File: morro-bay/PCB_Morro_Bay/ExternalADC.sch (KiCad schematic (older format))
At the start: 8 parts

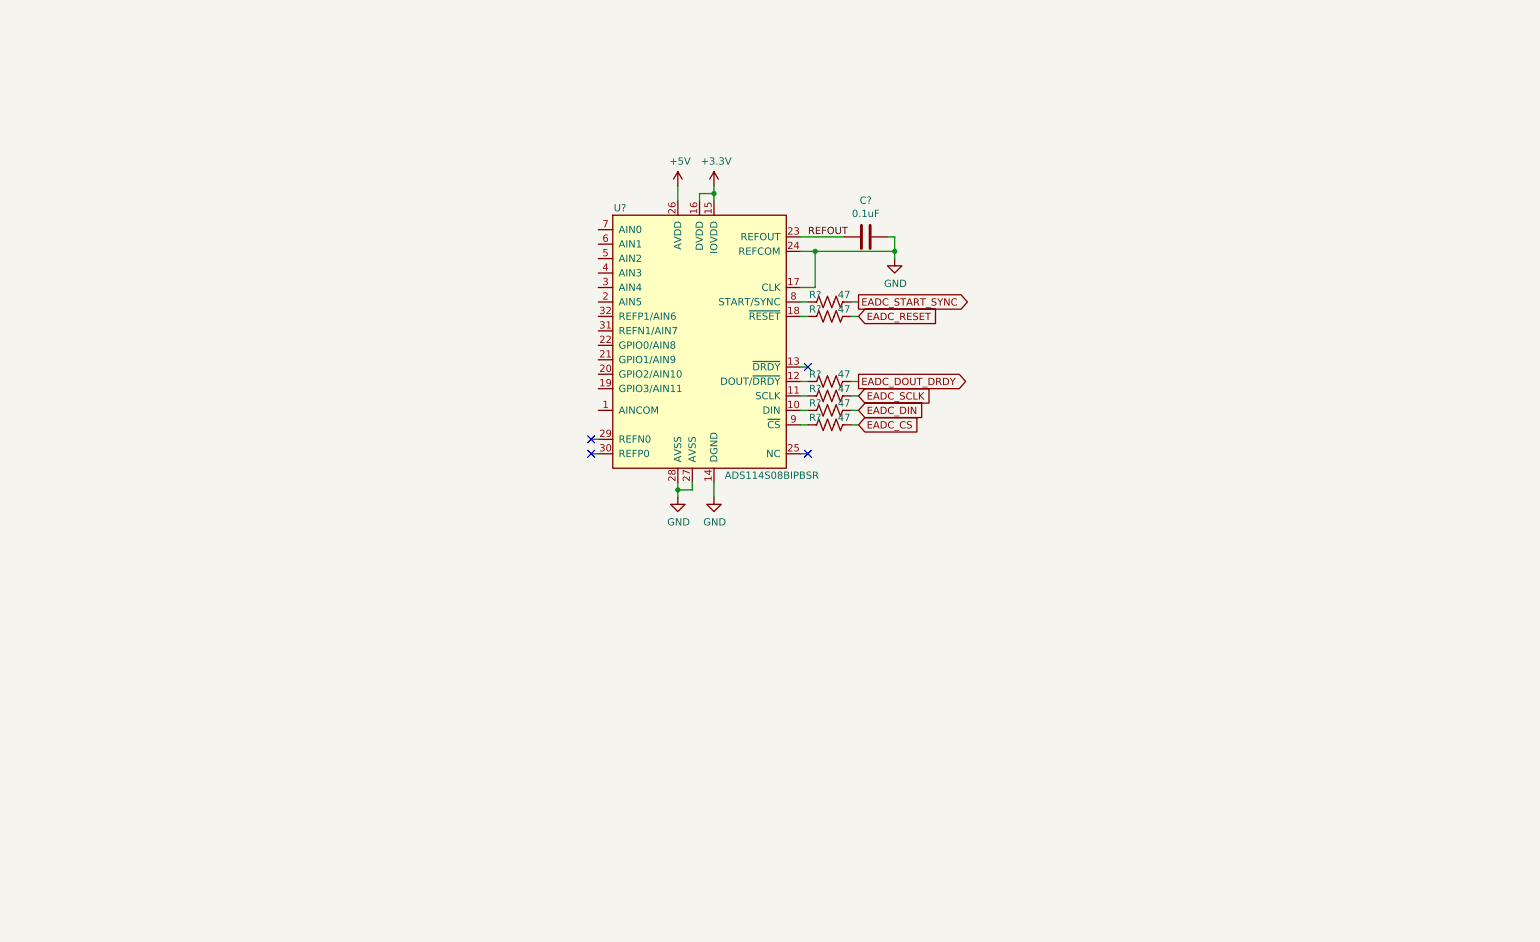
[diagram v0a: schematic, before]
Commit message: External ADC, SPI
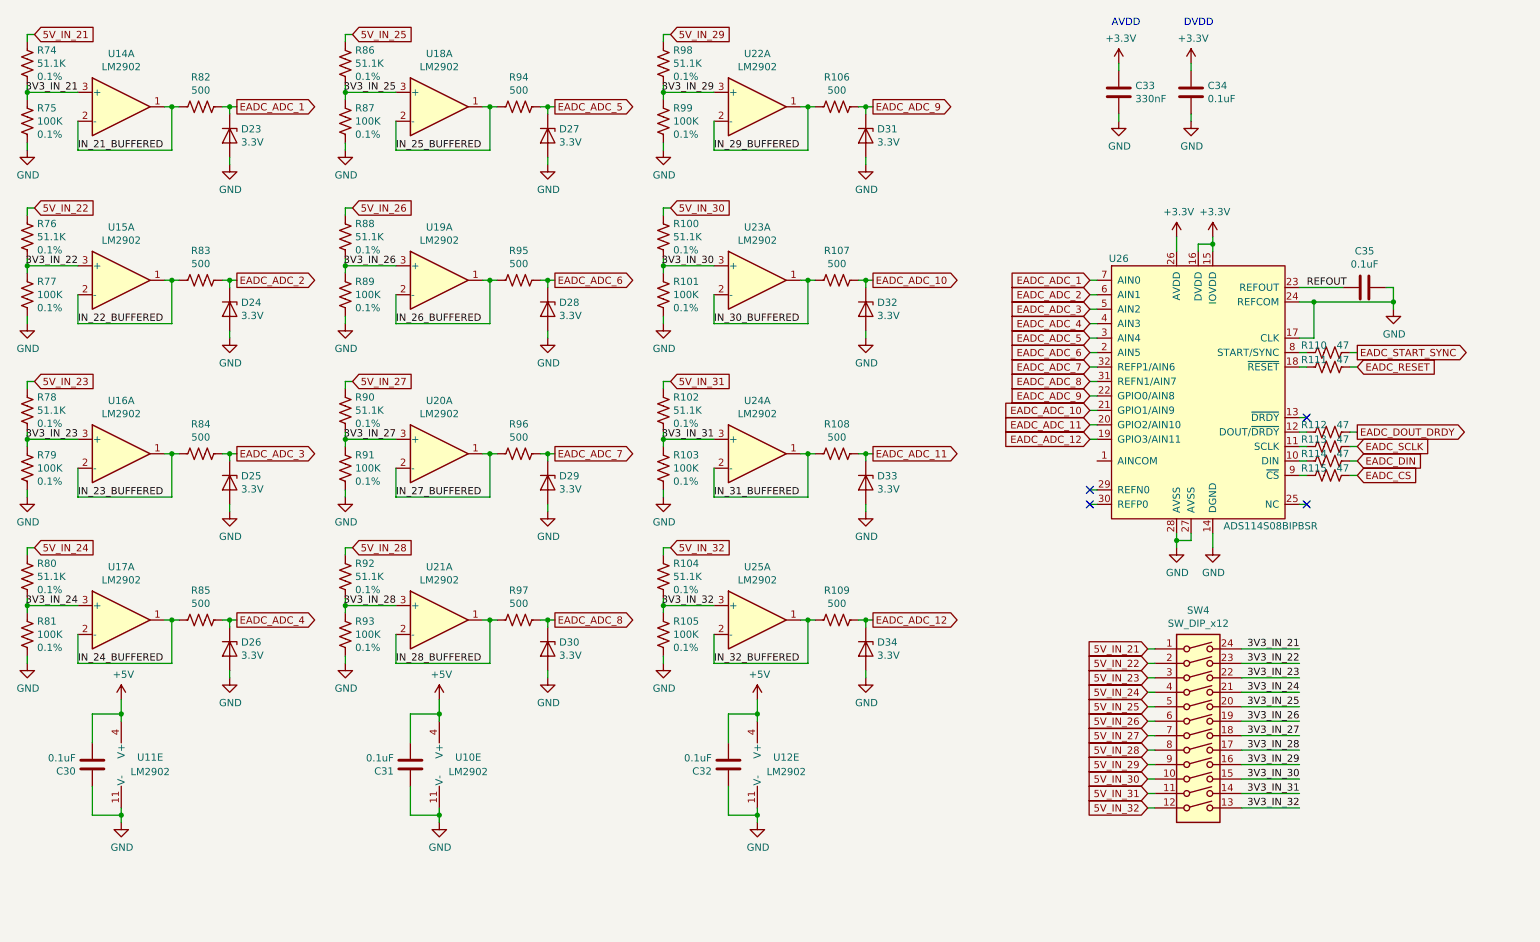
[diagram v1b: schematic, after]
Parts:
- added C30, C31, C32, C34: 0.1uF, symbol Device:C
- added C33: 330nF, symbol Device:C
- added D23, D24, D25, D26, D27, D28, D29, D30, D31, D32, D33, D34: 3.3V, symbol Device:D_Zener
- added R100, R102, R104, R74, R76, R78, R80, R86, R88, R90, R92, R98: 51.1K, symbol Device:R_US
- added R101, R103, R105, R75, R77, R79, R81, R87, R89, R91, R93, R99: 100K, symbol Device:R_US
- added R106, R107, R108, R109, R82, R83, R84, R85, R94, R95, R96, R97: 500, symbol Device:R_US
- added SW4: SW_DIP_x12, symbol Switch:SW_DIP_x12
- added U10, U11, U12, U14, U15, U16, U17, U18, U19, U20, U21, U22, U23, U24, U25: LM2902, symbol Amplifier_Operational:LM2902
- gave numbers to parts that had none: 8
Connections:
- net +3V3: now also U26.26 (AVDD), C33.1, C34.1
- net +5V: now also C30.2, C31.2, C32.2, U10.4 (V+), U11.4 (V+), U12.4 (V+); no longer U26.26 (AVDD)
- net GND: now also C30.1, C31.1, C32.1, C33.2, C34.2, D23.2 (A), D24.2 (A), D25.2 (A), D26.2 (A), D27.2 (A), D28.2 (A), D29.2 (A), D30.2 (A), D31.2 (A), D32.2 (A), D33.2 (A), D34.2 (A), R101.2, R103.2, R105.2, R75.2, R77.2, R79.2, R81.2, R87.2, R89.2, R91.2, R93.2, R99.2, U10.11 (V-), U11.11 (V-), U12.11 (V-)
- net EADC_ADC_12: now reaches U26.19 (GPIO3/AIN11)
- net EADC_ADC_12: now also D34.1 (K), R109.1
- net EADC_ADC_6: now reaches U26.2 (AIN5)
- net EADC_ADC_6: now also D28.1 (K), R95.1
- net EADC_ADC_11: now reaches U26.20 (GPIO2/AIN10)
- net EADC_ADC_11: now also D33.1 (K), R108.1
- net EADC_ADC_10: now reaches U26.21 (GPIO1/AIN9)
- net EADC_ADC_10: now also D32.1 (K), R107.1
- net EADC_ADC_9: now reaches U26.22 (GPIO0/AIN8)
- net EADC_ADC_9: now also D31.1 (K), R106.1
- net EADC_ADC_5: now reaches U26.3 (AIN4)
- net EADC_ADC_5: now also D27.1 (K), R94.1
- net EADC_ADC_8: now reaches U26.31 (REFN1/AIN7)
- net EADC_ADC_8: now also D30.1 (K), R97.1
- net EADC_ADC_7: now reaches U26.32 (REFP1/AIN6)
- net EADC_ADC_7: now also D29.1 (K), R96.1
- net EADC_ADC_4: now reaches U26.4 (AIN3)
- net EADC_ADC_4: now also D26.1 (K), R85.1
- net EADC_ADC_3: now reaches U26.5 (AIN2)
- net EADC_ADC_3: now also D25.1 (K), R84.1
- net EADC_ADC_2: now reaches U26.6 (AIN1)
- net EADC_ADC_2: now also D24.1 (K), R83.1
- net EADC_ADC_1: now reaches U26.7 (AIN0)
- net EADC_ADC_1: now also D23.1 (K), R82.1
- new net 3V3_IN_21: R74.2, R75.1, SW4.24, U14.3 (+)
- new net 3V3_IN_22: R76.2, R77.1, SW4.23, U15.3 (+)
- new net 3V3_IN_23: R78.2, R79.1, SW4.22, U16.3 (+)
- new net 3V3_IN_24: R80.2, R81.1, SW4.21, U17.3 (+)
- new net 3V3_IN_25: R86.2, R87.1, SW4.20, U18.3 (+)
- new net 3V3_IN_26: R88.2, R89.1, SW4.19, U19.3 (+)
- new net 3V3_IN_27: R90.2, R91.1, SW4.18, U20.3 (+)
- new net 3V3_IN_28: R92.2, R93.1, SW4.17, U21.3 (+)
- new net 3V3_IN_29: R98.2, R99.1, SW4.16, U22.3 (+)
- new net 3V3_IN_30: R100.2, R101.1, SW4.15, U23.3 (+)
- new net 3V3_IN_31: R102.2, R103.1, SW4.14, U24.3 (+)
- new net 3V3_IN_32: R104.2, R105.1, SW4.13, U25.3 (+)
- new net 5V_IN_21: R74.1, SW4.1
- new net 5V_IN_22: R76.1, SW4.2
- new net 5V_IN_23: R78.1, SW4.3
- new net 5V_IN_24: R80.1, SW4.4
- new net 5V_IN_25: R86.1, SW4.5
- new net 5V_IN_26: R88.1, SW4.6
- new net 5V_IN_27: R90.1, SW4.7
- new net 5V_IN_28: R92.1, SW4.8
- new net 5V_IN_29: R98.1, SW4.9
- new net 5V_IN_30: R100.1, SW4.10
- new net 5V_IN_31: R102.1, SW4.11
- new net 5V_IN_32: R104.1, SW4.12
- new net IN_21_BUFFERED: R82.2, U14.1, U14.2 (-)
- new net IN_22_BUFFERED: R83.2, U15.1, U15.2 (-)
- new net IN_23_BUFFERED: R84.2, U16.1, U16.2 (-)
- new net IN_24_BUFFERED: R85.2, U17.1, U17.2 (-)
- new net IN_25_BUFFERED: R94.2, U18.1, U18.2 (-)
- new net IN_26_BUFFERED: R95.2, U19.1, U19.2 (-)
- new net IN_27_BUFFERED: R96.2, U20.1, U20.2 (-)
- new net IN_28_BUFFERED: R97.2, U21.1, U21.2 (-)
- new net IN_29_BUFFERED: R106.2, U22.1, U22.2 (-)
- new net IN_30_BUFFERED: R107.2, U23.1, U23.2 (-)
- new net IN_31_BUFFERED: R108.2, U24.1, U24.2 (-)
- new net IN_32_BUFFERED: R109.2, U25.1, U25.2 (-)
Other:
- note added: "AVDD"
- note added: "DVDD"
- moved on the sheet: C35, R110, R111, R112, R113, R114, R115, U26

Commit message: Ready for initial sch review
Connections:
- net EADC_ADC_1: now also U26.2 (AIN5); no longer U26.7 (AIN0)
- net EADC_ADC_10: now also U26.22 (GPIO0/AIN8); no longer U26.21 (GPIO1/AIN9)
- net EADC_ADC_11: now also U26.31 (REFN1/AIN7); no longer U26.20 (GPIO2/AIN10)
- net EADC_ADC_12: now also U26.32 (REFP1/AIN6); no longer U26.19 (GPIO3/AIN11)
- net EADC_ADC_2: now also U26.3 (AIN4); no longer U26.6 (AIN1)
- net EADC_ADC_3: now also U26.4 (AIN3); no longer U26.5 (AIN2)
- net EADC_ADC_4: now also U26.5 (AIN2); no longer U26.4 (AIN3)
- net EADC_ADC_5: now also U26.6 (AIN1); no longer U26.3 (AIN4)
- net EADC_ADC_6: now also U26.7 (AIN0); no longer U26.2 (AIN5)
- net EADC_ADC_7: now also U26.19 (GPIO3/AIN11); no longer U26.32 (REFP1/AIN6)
- net EADC_ADC_8: now also U26.20 (GPIO2/AIN10); no longer U26.31 (REFN1/AIN7)
- net EADC_ADC_9: now also U26.21 (GPIO1/AIN9); no longer U26.22 (GPIO0/AIN8)
- net GND: now also U26.1 (AINCOM)
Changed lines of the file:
@@
 Wire Wire Line
 	5300 1950 5250 1950
+Text GLabel 8200 2950 0    50   Input ~ 0
+EADC_ADC_1
+Wire Wire Line
+	8200 2450 8250 2450
+Text GLabel 8200 2850 0    50   Input ~ 0
+EADC_ADC_2
+Wire Wire Line
+	8200 2550 8250 2550
+Text GLabel 8200 2750 0    50   Input ~ 0
+EADC_ADC_3
+Wire Wire Line
+	8200 2650 8250 2650
+Text GLabel 8200 2650 0    50   Input ~ 0
+EADC_ADC_4
+Wire Wire Line
+	8200 2750 8250 2750
+Text GLabel 8200 2550 0    50   Input ~ 0
+EADC_ADC_5
+Wire Wire Line
+	8200 2850 8250 2850
 Text GLabel 8200 2450 0    50   Input ~ 0
-EADC_ADC_1
-Wire Wire Line
-	8200 2450 8250 2450
-Text GLabel 8200 2550 0    50   Input ~ 0
-EADC_ADC_2
-Wire Wire Line
-	8200 2550 8250 2550
-Text GLabel 8200 2650 0    50   Input ~ 0
-EADC_ADC_3
-Wire Wire Line
-	8200 2650 8250 2650
-Text GLabel 8200 2750 0    50   Input ~ 0
-EADC_ADC_4
-Wire Wire Line
-	8200 2750 8250 2750
-Text GLabel 8200 2850 0    50   Input ~ 0
-EADC_ADC_5
-Wire Wire Line
-	8200 2850 8250 2850
-Text GLabel 8200 2950 0    50   Input ~ 0
 EADC_ADC_6
 Wire Wire Line
 	8200 2950 8250 2950
+Text GLabel 8200 3550 0    50   Input ~ 0
+EADC_ADC_7
+Wire Wire Line
+	8200 3050 8250 3050
+Text GLabel 8200 3450 0    50   Input ~ 0
+EADC_ADC_8
+Wire Wire Line
+	8200 3150 8250 3150
+Text GLabel 8200 3350 0    50   Input ~ 0
+EADC_ADC_9
+Wire Wire Line
+	8200 3250 8250 3250
+Text GLabel 8200 3250 0    50   Input ~ 0
+EADC_ADC_10
+Wire Wire Line
+	8200 3350 8250 3350
+Text GLabel 8200 3150 0    50   Input ~ 0
+EADC_ADC_11
+Wire Wire Line
+	8200 3450 8250 3450
 Text GLabel 8200 3050 0    50   Input ~ 0
-EADC_ADC_7
-Wire Wire Line
-	8200 3050 8250 3050
-Text GLabel 8200 3150 0    50   Input ~ 0
-EADC_ADC_8
-Wire Wire Line
-	8200 3150 8250 3150
-Text GLabel 8200 3250 0    50   Input ~ 0
-EADC_ADC_9
-Wire Wire Line
-	8200 3250 8250 3250
-Text GLabel 8200 3350 0    50   Input ~ 0
-EADC_ADC_10
-Wire Wire Line
-	8200 3350 8250 3350
-Text GLabel 8200 3450 0    50   Input ~ 0
-EADC_ADC_11
-Wire Wire Line
-	8200 3450 8250 3450
-Text GLabel 8200 3550 0    50   Input ~ 0
 EADC_ADC_12
 Wire Wire Line
@@
 Text Notes 8850 700  0    50   ~ 0
 DVDD
+Wire Wire Line
+	8250 3700 8050 3700
+Wire Wire Line
+	8050 3700 8050 3750
+$Comp
+L power:GND #PWR?
+U 1 1 5EE946F3
+P 8050 3750
+F 0 "#PWR?" H 8050 3500 50  0001 C CNN
+F 1 "GND" H 8055 3577 50  0000 C CNN
+F 2 "" H 8050 3750 50  0001 C CNN
+F 3 "" H 8050 3750 50  0001 C CNN
+	1    8050 3750
+	1    0    0    -1
+$EndComp
 $EndSCHEMATC

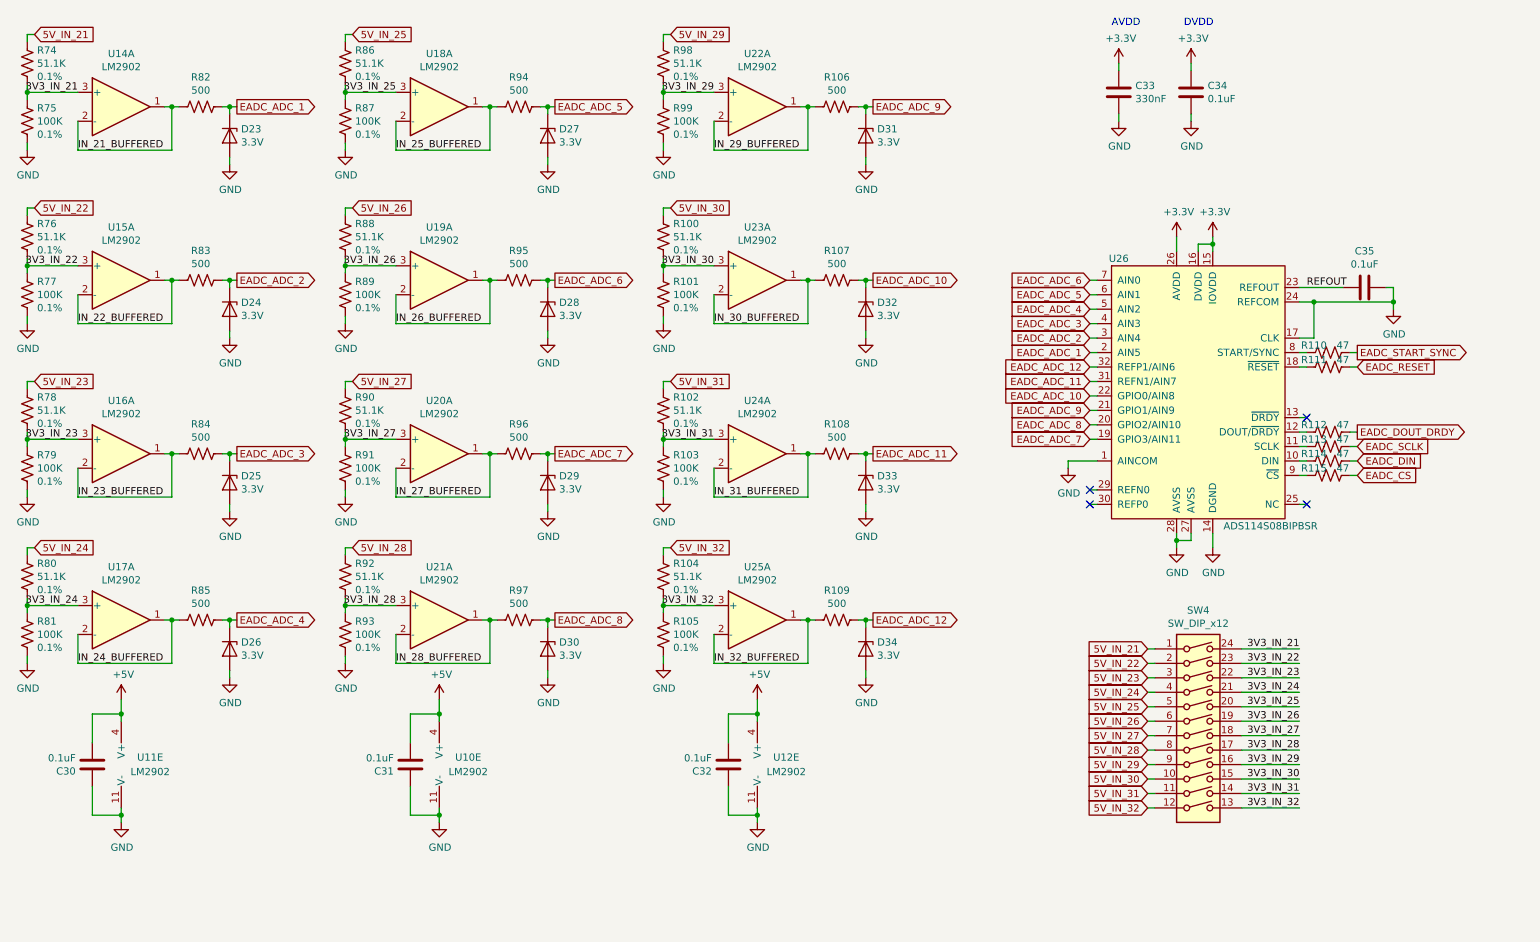
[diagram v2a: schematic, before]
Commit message: Work on BOM
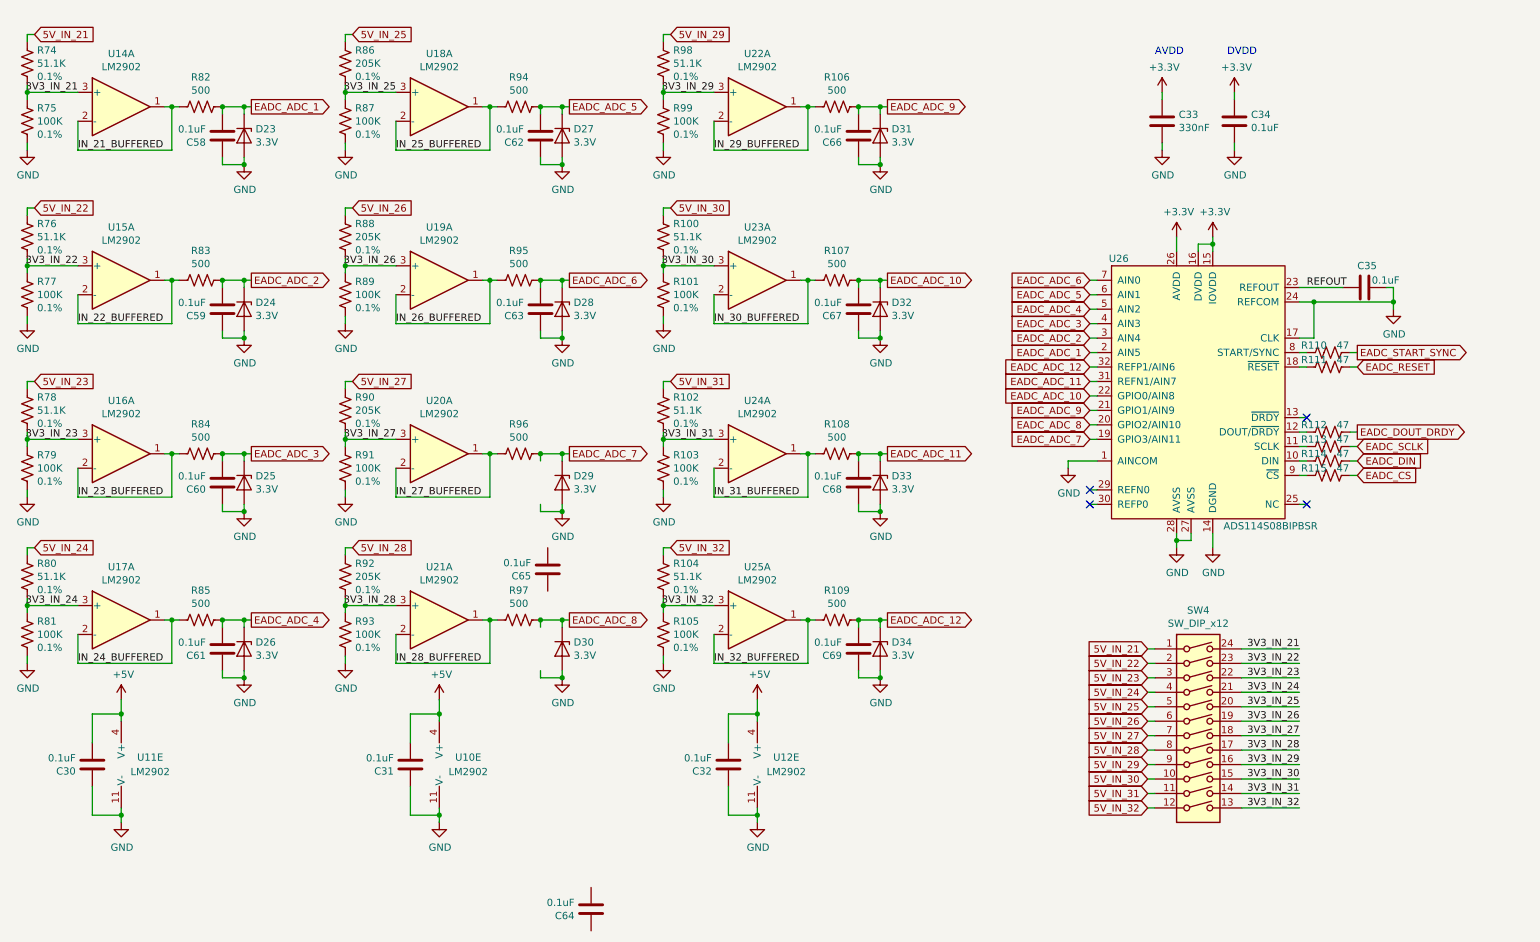
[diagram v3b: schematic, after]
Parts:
- added C58, C59, C60, C61, C62, C63, C64, C65, C66, C67, C68, C69: 0.1uF, Capacitor_SMD:C_0603_1608Metric_Pad1.05x0.95mm_HandSolder, symbol Device:C
- C30, C31, C32, C34, C35: footprint (none) -> Capacitor_SMD:C_0603_1608Metric_Pad1.05x0.95mm_HandSolder; Digikey (none) -> https://www.digikey.ca/product-detail/en/yageo/CC0603KRX7R8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; Part Number (none) -> CC0603KRX7R8BB104
- D23, D24, D25, D26, D27, D28, D29, D30, D31, D32, D33, D34: footprint (none) -> Diode_SMD:D_SOD-323_HandSoldering; Digikey (none) -> https://www.digikey.ca/product-detail/en/on-semiconductor/M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; Part Number (none) -> MM3Z3V3ST1G
- R86, R88, R90, R92: value 51.1K -> 205K
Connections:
- net EADC_ADC_1: now also C58.2
- net EADC_ADC_10: now also C67.2
- net EADC_ADC_11: now also C68.2
- net EADC_ADC_12: now also C69.2
- net EADC_ADC_2: now also C59.2
- net EADC_ADC_3: now also C60.2
- net EADC_ADC_4: now also C61.2
- net EADC_ADC_5: now also C62.2
- net EADC_ADC_6: now also C63.2
- net EADC_ADC_9: now also C66.2
- net GND: now also C58.1, C59.1, C60.1, C61.1, C62.1, C63.1, C66.1, C67.1, C68.1, C69.1
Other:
- moved on the sheet: C33

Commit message: More BOM
And if that don't work, use more gun.
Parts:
- removed R112, R113, R114, R115: 47, symbol Device:R_US
- C33: footprint (none) -> Capacitor_SMD:C_0603_1608Metric_Pad1.05x0.95mm_HandSolder; Digikey (none) -> https://www.digikey.ca/en/products/detail/kemet/C0603C331J5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; Part Number (none) -> C0603C331J5GACTU
- R100, R102, R104, R98: value 51.1K -> 47; footprint (none) -> Resistor_SMD:R_0603_1608Metric_Pad1.05x0.95mm_HandSolder; Digikey (none) -> https://www.digikey.ca/product-detail/en/stackpole-electron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; Part Number (none) -> RMCF0603FT47R0; Tolerance 0.1% -> (none)
- R110, R111: footprint (none) -> Resistor_SMD:R_0603_1608Metric_Pad1.05x0.95mm_HandSolder; Digikey (none) -> https://www.digikey.ca/product-detail/en/stackpole-electron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; Part Number (none) -> RMCF0603FT47R0
- U26: Digikey (none) -> https://www.digikey.ca/product-detail/en/texas-instruments/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; Part Number (none) -> ADS114S08BIPBSR
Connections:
- net 3V3_IN_29: no longer R98.2, R99.1, U22.3 (+)
- net 3V3_IN_30: no longer R100.2, R101.1, U23.3 (+)
- net 3V3_IN_31: no longer R102.2, R103.1, U24.3 (+)
- net 3V3_IN_32: no longer R104.2, R105.1, U25.3 (+)
- net 5V_IN_21: no longer R74.1
- net 5V_IN_22: no longer R76.1
- net 5V_IN_23: no longer R78.1
- net 5V_IN_24: no longer R80.1
- net 5V_IN_25: no longer R86.1
- net 5V_IN_26: no longer R88.1
- net 5V_IN_27: no longer R90.1
- net 5V_IN_28: no longer R92.1
- net 5V_IN_29: no longer R98.1
- net 5V_IN_30: no longer R100.1
- net 5V_IN_31: no longer R102.1
- net 5V_IN_32: no longer R104.1
- net EADC_ADC_7: now also C64.2
- net EADC_ADC_8: now also C65.2
- net EADC_CS: now also R111.2
- net EADC_DIN: now also R104.2
- net EADC_DOUT_DRDY: now also R100.2
- net EADC_RESET: now also R98.2; no longer R111.2
- net EADC_SCLK: now also R102.2
- net GND: now also C64.1, C65.1
- net at U26.10 (DIN): now also R104.1
- net at U26.11 (SCLK): now also R102.1
- net at U26.12 (DOUT/~DRDY~): now also R100.1
- net at U26.18 (~RESET~): now also R98.1; no longer R111.1
- net at U26.9 (~CS~): now also R111.1
- new net 10V_IN_7: R86.1
- new net 10V_IN_8: R88.1
- new net 10V_IN_9: R90.1, R92.1
- new net 5V_IN_13: R74.1
- new net 5V_IN_14: R76.1
- new net 5V_IN_15: R78.1
- new net 5V_IN_16: R80.1
- new net RES_IN_1: R99.1, U22.3 (+)
- new net RES_IN_2: R101.1, U23.3 (+)
- new net RES_IN_3: R103.1, U24.3 (+)
- new net RES_IN_4: R105.1, U25.3 (+)
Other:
- moved on the sheet: C65
